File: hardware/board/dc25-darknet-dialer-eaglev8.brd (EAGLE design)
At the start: 101.6 x 101.6 mm, 86 parts, among them J1 MF-CON-MICROUSB-RIGHT, SW1 RESET, U1 BU33SD5WG-TR, U2 MCP73831T-5ACI/OT, U3 SOP22FLAT, Y1 CSTCE8M00G52-R0

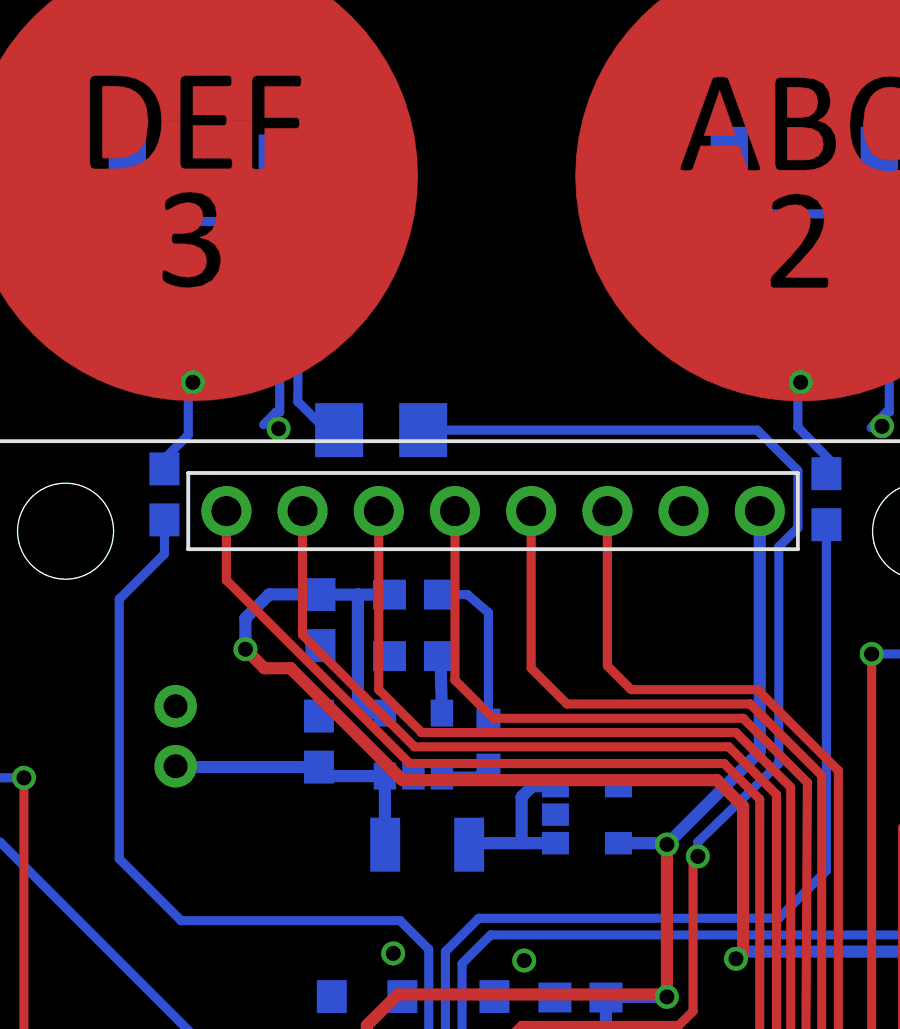
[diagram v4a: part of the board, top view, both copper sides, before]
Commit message: Added on/off switch
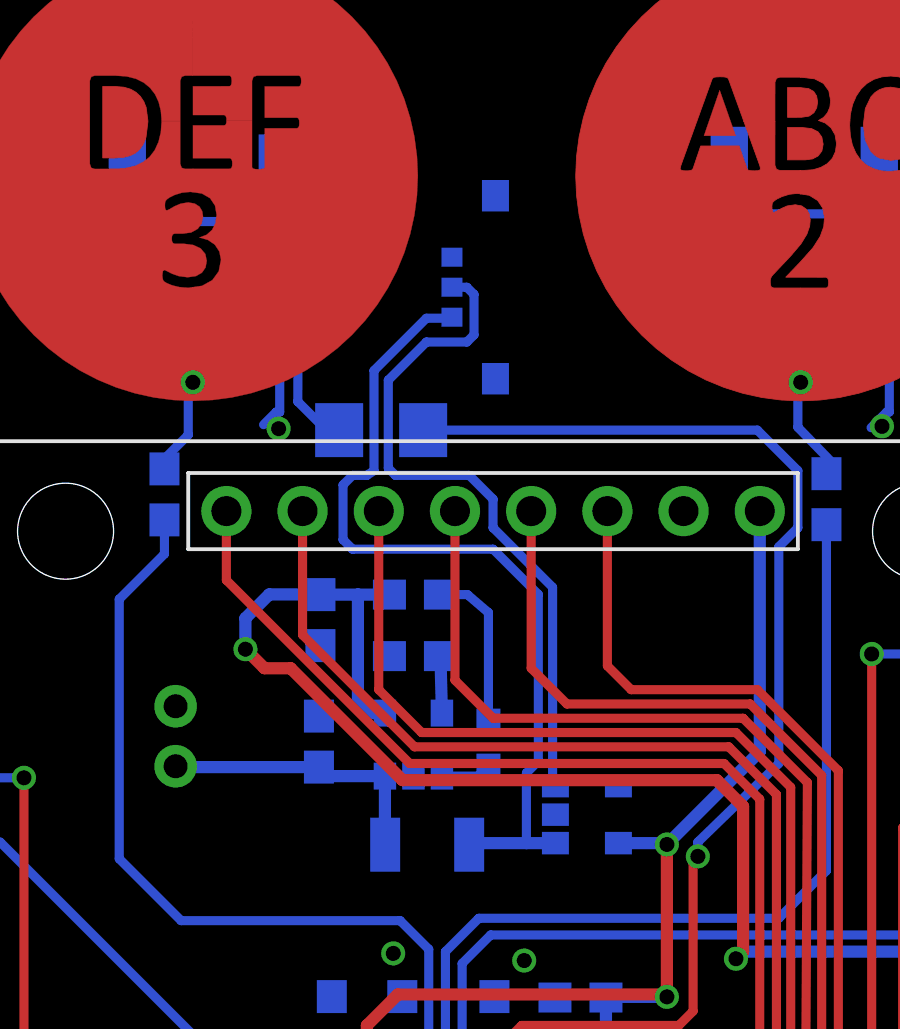
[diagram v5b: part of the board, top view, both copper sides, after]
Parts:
- added U$11: SWITCH_SPDT, darknet_parts_library:SPDT_SSAJ120100
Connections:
- new net N$32: U$11.C, U1.3
- net N$30: now also U$11.2; no longer U1.3
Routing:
- net N$32: track 0.00 -> 23.0 mm
- net N$30: track 5.71 -> 28.3 mm
